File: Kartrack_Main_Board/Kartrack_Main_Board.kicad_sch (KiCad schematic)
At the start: 0 parts

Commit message: pcb
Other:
- sheet CONN ports: added PF6, PG6_STBY_GPS; removed PF6_STBY_GPS, PG6
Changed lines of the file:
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@@
-			)
-		)
-		(pin "PIO_SPI2_NSS" input
-			(at 241.3 68.58 180)
-			(effects
-				(font
-					(size 1.27 1.27)
-				)
-				(justify left)
 			)
 		)
@@
 			)
 		)
-		(pin "PA8" input
-			(at 241.3 101.6 180)
-			(effects
-				(font
-					(size 1.27 1.27)
-				)
-				(justify left)
-			)
-		)
-		(pin "PA15" input
-			(at 241.3 104.14 180)
-			(effects
-				(font
-					(size 1.27 1.27)
-				)
-				(justify left)
-			)
-		)
 		(pin "PI3" input
 			(at 241.3 73.66 180)
-			(effects
-				(font
-					(size 1.27 1.27)
-				)
-				(justify left)
-			)
-		)
-		(pin "PG6" input
-			(at 241.3 76.2 180)
-			(effects
-				(font
-					(size 1.27 1.27)
-				)
-				(justify left)
-			)
-		)
-		(pin "PG7" input
-			(at 241.3 78.74 180)
-			(effects
-				(font
-					(size 1.27 1.27)
-				)
-				(justify left)
-			)
-		)
-		(pin "PI2" input
-			(at 241.3 81.28 180)
 			(effects
 				(font
@@
 			)
 		)
-		(pin "PF6_STBY_GPS" input
+		(pin "PF8_LORA_RST" input
+			(at 241.3 86.36 180)
+			(effects
+				(font
+					(size 1.27 1.27)
+				)
+				(justify left)
+			)
+		)
+		(pin "PG6_STBY_GPS" input
 			(at 241.3 106.68 180)
 			(effects
@@
 			)
 		)
-		(pin "PF8_LORA_RST" input
-			(at 241.3 86.36 180)
+		(pin "PA8" input
+			(at 241.3 81.28 180)
 			(effects
 				(font
+					(size 1.27 1.27)
+				)
+				(justify left)
+			)
+		)
+		(pin "PIO_SPI2_NSS" input
+			(at 241.3 68.58 180)
+			(effects
+				(font
+					(size 1.27 1.27)
+				)
+				(justify left)
+			)
+		)
+		(pin "PF6" input
+			(at 241.3 104.14 180)
+			(effects
+				(font
+					(size 1.27 1.27)
+				)
+				(justify left)
+			)
+		)
+		(pin "PA15" input
+			(at 241.3 78.74 180)
+			(effects
+				(font
+					(size 1.27 1.27)
+				)
+				(justify left)
+			)
+		)
+		(pin "PI2" input
+			(at 241.3 76.2 180)
+			(effects
+				(font
+					(size 1.27 1.27)
+				)
+				(justify left)
+			)
+		)
+		(pin "PG7" input
+			(at 241.3 101.6 180)
+			(effects
+				(font

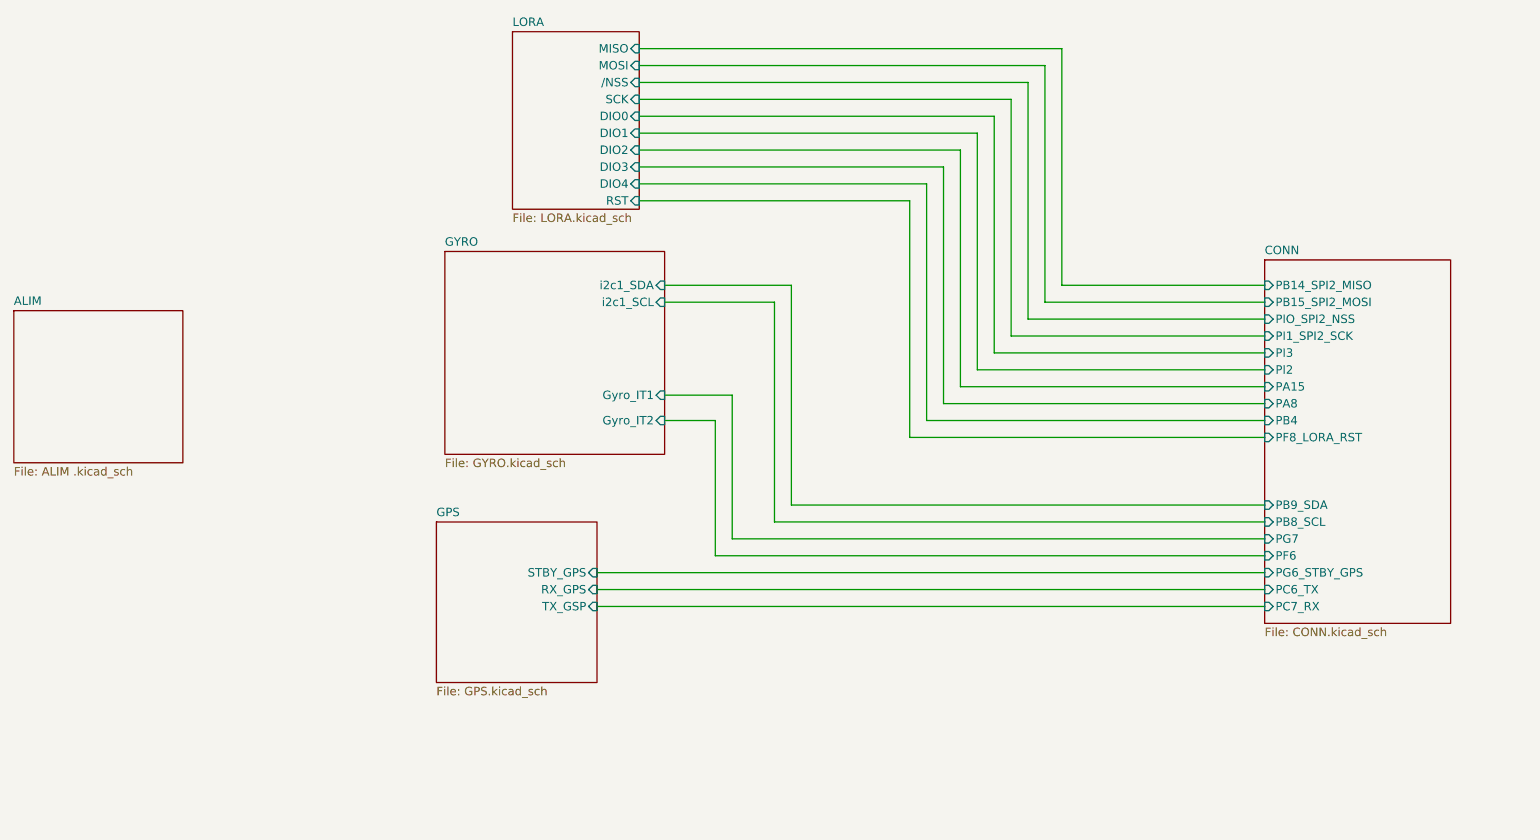
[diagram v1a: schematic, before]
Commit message: add adc batt
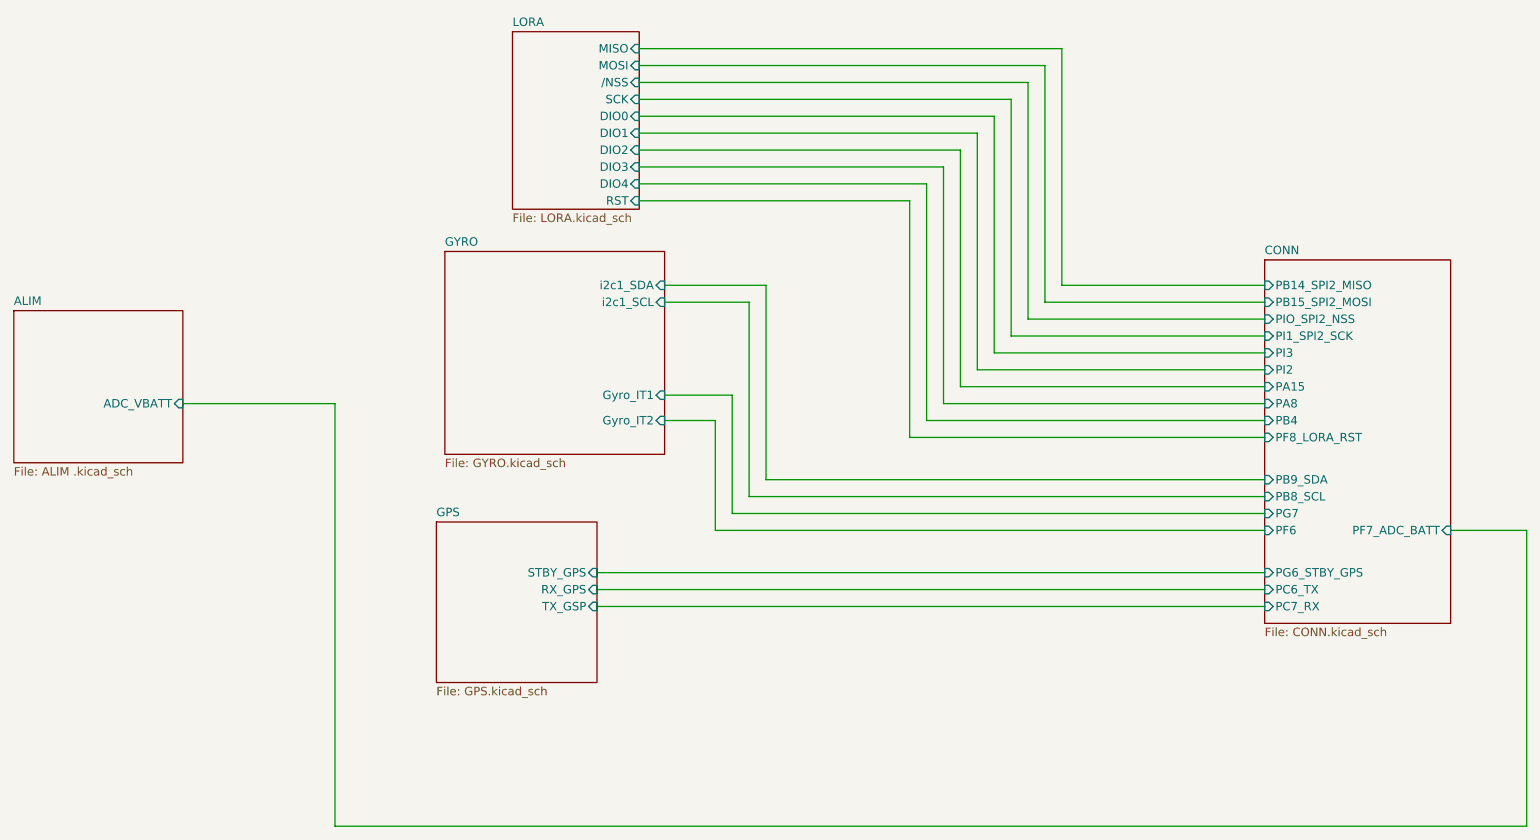
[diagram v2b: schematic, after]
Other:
- sheet ALIM ports: added ADC_VBATT; removed none
- sheet CONN ports: added PF7_ADC_BATT; removed none
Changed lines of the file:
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@@
 	(wire
 		(pts
-			(xy 158.75 104.14) (xy 241.3 104.14)
+			(xy 158.75 100.33) (xy 241.3 100.33)
 		)
 		(stroke
@@
 	(wire
 		(pts
-			(xy 158.75 83.82) (xy 158.75 104.14)
+			(xy 158.75 83.82) (xy 158.75 100.33)
 		)
 		(stroke
@@
 	(wire
 		(pts
-			(xy 170.18 63.5) (xy 170.18 96.52)
-		)
-		(stroke
-			(width 0)
-			(type default)
-		)
-	)
-	(wire
-		(pts
-			(xy 151.13 66.04) (xy 167.64 66.04)
+			(xy 166.37 63.5) (xy 166.37 92.71)
+		)
+		(stroke
+			(width 0)
+			(type default)
+		)
+	)
+	(wire
+		(pts
+			(xy 151.13 66.04) (xy 163.83 66.04)
 		)
 		(stroke
@@
 	(wire
 		(pts
-			(xy 161.29 101.6) (xy 241.3 101.6)
+			(xy 269.24 100.33) (xy 280.67 100.33)
+		)
+		(stroke
+			(width 0)
+			(type default)
+		)
+	)
+	(wire
+		(pts
+			(xy 161.29 97.79) (xy 241.3 97.79)
 		)
 		(stroke
@@
 	(wire
 		(pts
-			(xy 170.18 96.52) (xy 241.3 96.52)
+			(xy 78.74 81.28) (xy 101.6 81.28)
+		)
+		(stroke
+			(width 0)
+			(type default)
+		)
+	)
+	(wire
+		(pts
+			(xy 166.37 92.71) (xy 241.3 92.71)
+		)
+		(stroke
+			(width 0)
+			(type default)
+		)
+	)
+	(wire
+		(pts
+			(xy 101.6 144.78) (xy 280.67 144.78)
 		)
 		(stroke
@@
 	(wire
 		(pts
-			(xy 167.64 99.06) (xy 241.3 99.06)
+			(xy 163.83 95.25) (xy 241.3 95.25)
 		)
 		(stroke
@@
 	(wire
 		(pts
+			(xy 280.67 100.33) (xy 280.67 144.78)
+		)
+		(stroke
+			(width 0)
+			(type default)
+		)
+	)
+	(wire
+		(pts
 			(xy 187.96 86.36) (xy 241.3 86.36)
 		)
@@
 	(wire
 		(pts
-			(xy 161.29 80.01) (xy 161.29 101.6)
+			(xy 161.29 80.01) (xy 161.29 97.79)
+		)
+		(stroke
+			(width 0)
+			(type default)
+		)
+	)
+	(wire
+		(pts
+			(xy 101.6 81.28) (xy 101.6 144.78)
 		)
 		(stroke
@@
 	(wire
 		(pts
-			(xy 167.64 66.04) (xy 167.64 99.06)
+			(xy 163.83 66.04) (xy 163.83 95.25)
 		)
 		(stroke
@@
 	(wire
 		(pts
-			(xy 151.13 63.5) (xy 170.18 63.5)
+			(xy 151.13 63.5) (xy 166.37 63.5)
 		)
 		(stroke
@@
 		)
 		(pin "PB8_SCL" input
-			(at 241.3 99.06 180)
+			(at 241.3 95.25 180)
 			(effects
 				(font
@@
 		)
 		(pin "PB9_SDA" input
-			(at 241.3 96.52 180)
+			(at 241.3 92.71 180)
 			(effects
 				(font
@@
 		)
 		(pin "PF6" input
-			(at 241.3 104.14 180)
+			(at 241.3 100.33 180)
 			(effects
 				(font
@@
 		)
 		(pin "PG7" input
-			(at 241.3 101.6 180)
-			(effects
-				(font
-					(size 1.27 1.27)
-				)
-				(justify left)
+			(at 241.3 97.79 180)
+			(effects
+				(font
+					(size 1.27 1.27)
+				)
+				(justify left)
+			)
+		)
+		(pin "PF7_ADC_BATT" input
+			(at 269.24 100.33 0)
+			(effects
+				(font
+					(size 1.27 1.27)
+				)
+				(justify right)
 			)
 		)
@@
 			)
 		)
+		(pin "ADC_VBATT" input
+			(at 78.74 81.28 0)
+			(effects
+				(font
+					(size 1.27 1.27)
+				)
+				(justify right)
+			)
+		)
